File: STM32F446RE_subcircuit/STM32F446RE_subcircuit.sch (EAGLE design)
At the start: 47 parts, among them IC1 74AC126N, IC2 LD117AS33TR, IC3 74AC126N, IC4 74HC04N, IC5 74AC126N, U1 STM32F446RE, X1 MSTBA2, X2 32.768kHz, X3 8MHz

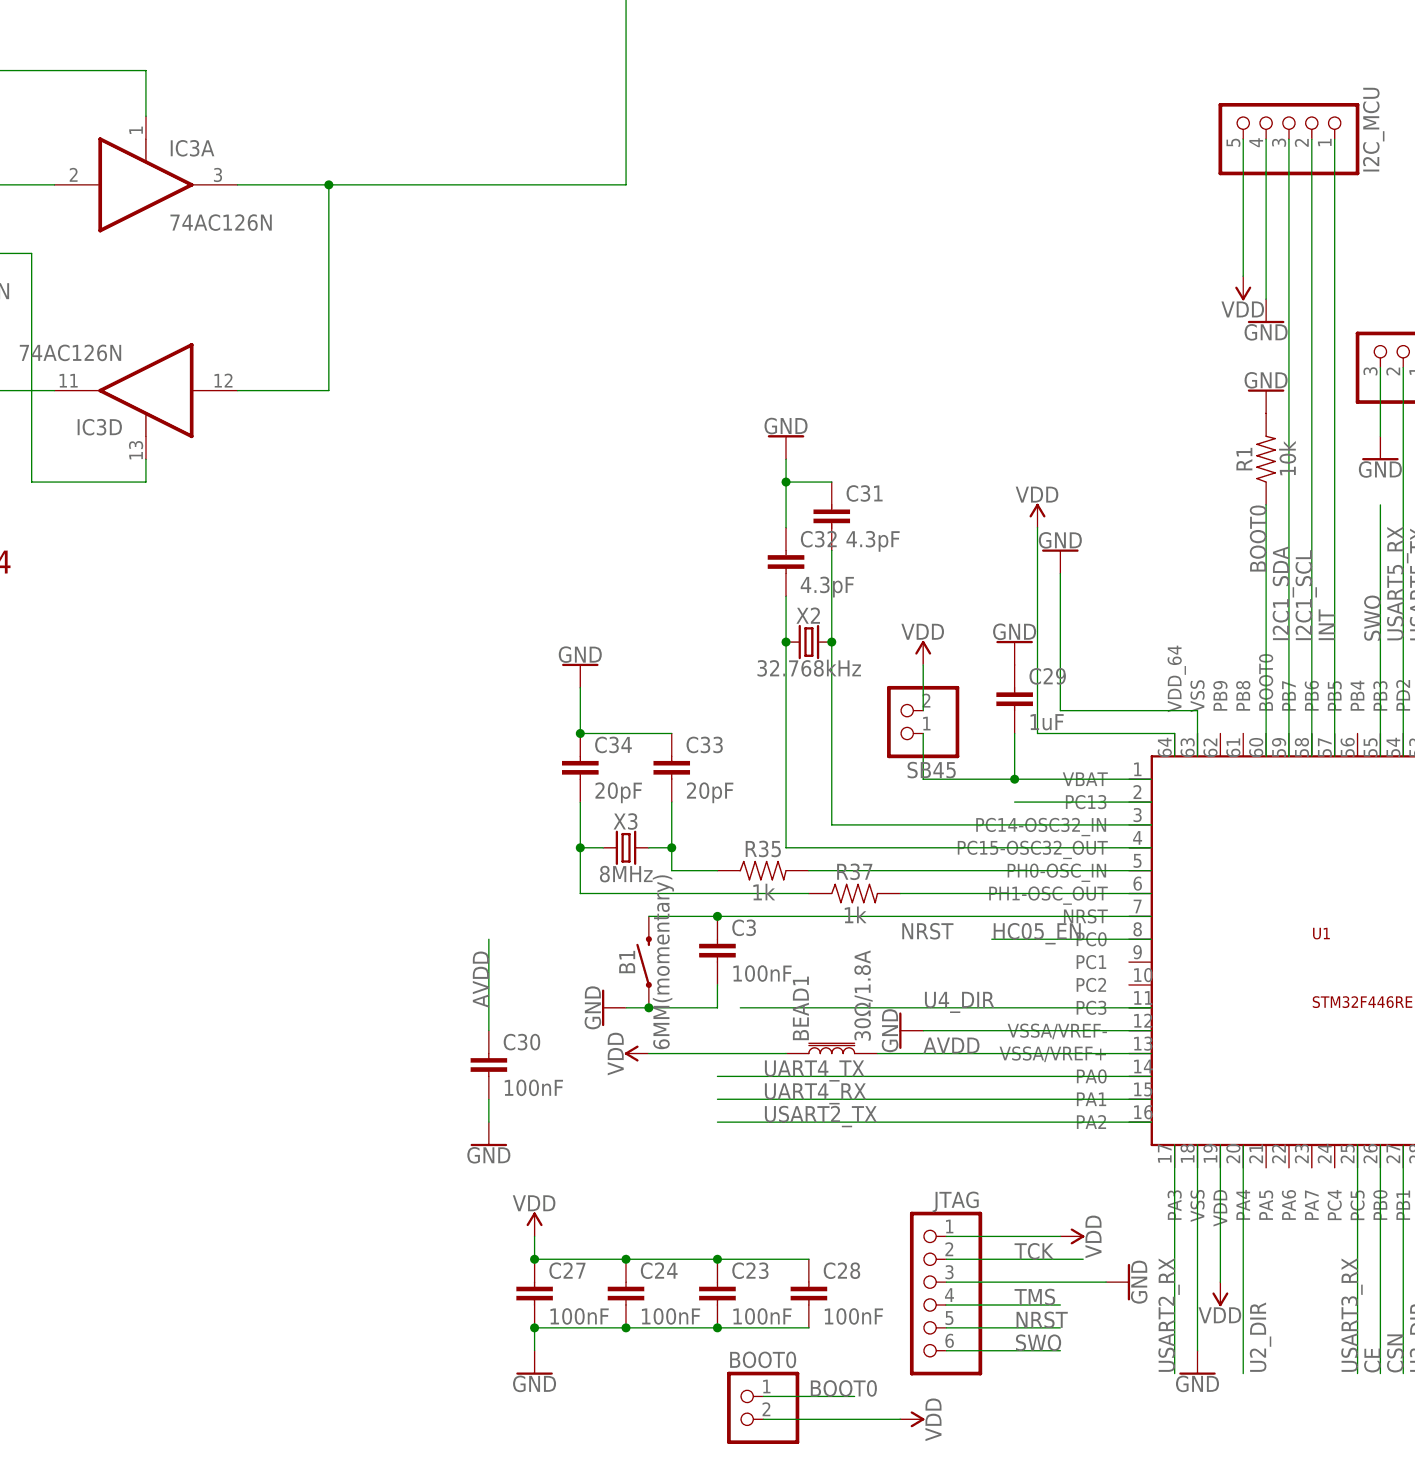
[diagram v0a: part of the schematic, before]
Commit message: Library added, Dip switch and power monitoring header was added
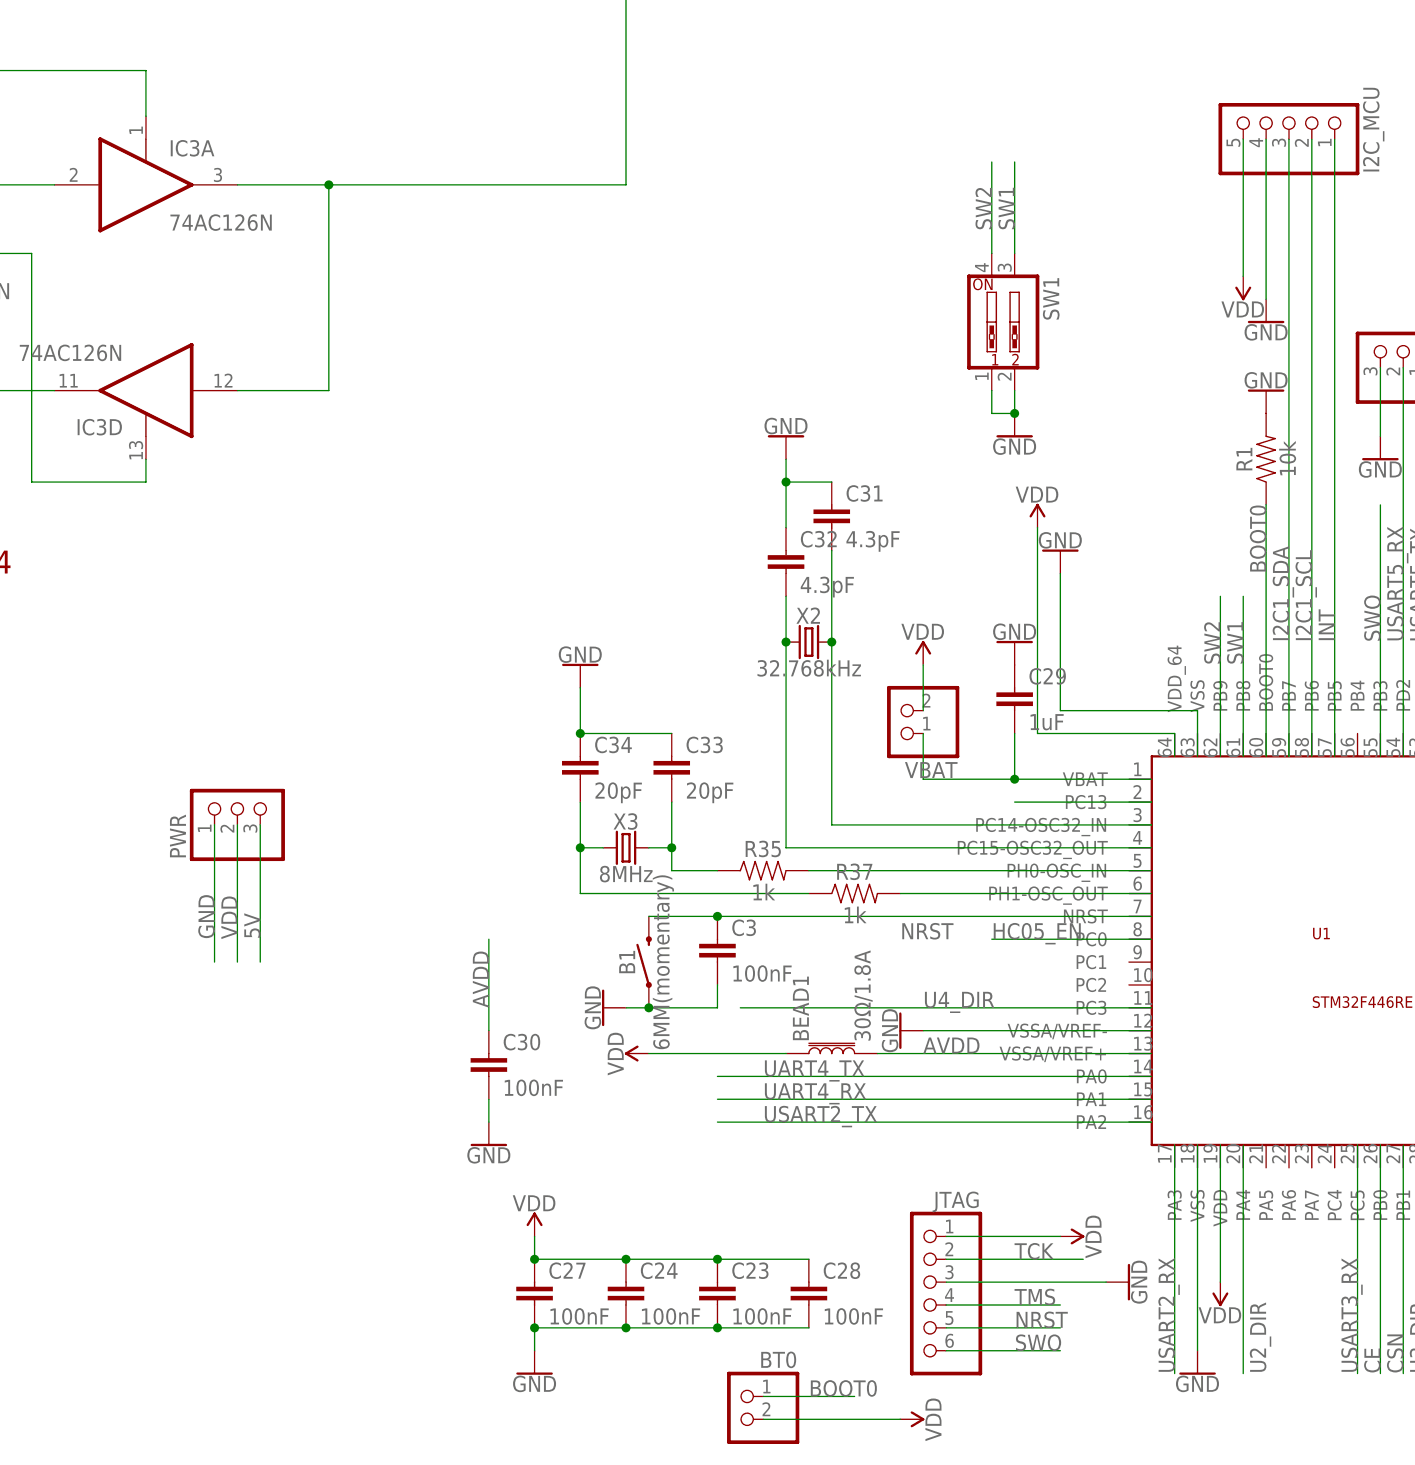
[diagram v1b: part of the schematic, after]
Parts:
- added PWR: (no value), pinhead:PINHD-1X3
- added SW1: (no value), special:SW_DIP-2
- renumbered BOOT0 to BT0, SB45 to VBAT
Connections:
- new net SW1: SW1.3, U1.PB8
- new net SW2: SW1.4, U1.PB9
- net 5V: now also PWR.3
- net GND: now also PWR.1, SW1.1, SW1.2
- net VDD: now also PWR.2
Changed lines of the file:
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@@
 <part name="R35" library="SparkFun-Resistors" deviceset="10KOHM" device="-HORIZ-1/4W-1%" value="1k"/>
 <part name="R37" library="SparkFun-Resistors" deviceset="10KOHM" device="-HORIZ-1/4W-1%" value="1k"/>
-<part name="SB45" library="pinhead" library_urn="urn:adsk.eagle:library:325" deviceset="PINHD-1X2" device="" package3d_urn="urn:adsk.eagle:package:22435/2"/>
+<part name="VBAT" library="pinhead" library_urn="urn:adsk.eagle:library:325" deviceset="PINHD-1X2" device="" package3d_urn="urn:adsk.eagle:package:22435/2"/>
 <part name="SUPPLY1" library="SparkFun-PowerSymbols" deviceset="VDD" device=""/>
 <part name="C29" library="ee2parts" deviceset="C" device="5P" value="1uF"/>
@@
 <part name="JTAG" library="pinhead" library_urn="urn:adsk.eagle:library:325" deviceset="PINHD-1X6" device="" package3d_urn="urn:adsk.eagle:package:22472/2"/>
 <part name="SUPPLY7" library="SparkFun-PowerSymbols" deviceset="VDD" device=""/>
-<part name="BOOT0" library="pinhead" library_urn="urn:adsk.eagle:library:325" deviceset="PINHD-1X2" device="" package3d_urn="urn:adsk.eagle:package:22435/2"/>
+<part name="BT0" library="pinhead" library_urn="urn:adsk.eagle:library:325" deviceset="PINHD-1X2" device="" package3d_urn="urn:adsk.eagle:package:22435/2"/>
 <part name="SUPPLY21" library="SparkFun-PowerSymbols" deviceset="VDD" device=""/>
 <part name="SUPPLY22" library="SparkFun-PowerSymbols" deviceset="VDD" device=""/>
@@
 <part name="NRF" library="pinhead" library_urn="urn:adsk.eagle:library:325" deviceset="PINHD-2X4" device="" package3d_urn="urn:adsk.eagle:package:22461/2"/>
 <part name="C4" library="ee2parts" deviceset="C" device="2.5P" value="100nF"/>
+<part name="SW1" library="special" library_urn="urn:adsk.eagle:library:367" deviceset="SW_DIP-2" device="" package3d_urn="urn:adsk.eagle:package:26654/2"/>
+<part name="GND24" library="SparkFun-PowerSymbols" deviceset="GND" device=""/>
+<part name="PWR" library="pinhead" library_urn="urn:adsk.eagle:library:325" deviceset="PINHD-1X3" device="" package3d_urn="urn:adsk.eagle:package:22458/2"/>
 </parts>
 <sheets>
@@
 <instance part="R35" gate="G$1" x="-63.5" y="10.16"/>
 <instance part="R37" gate="G$1" x="-53.34" y="7.62"/>
-<instance part="SB45" gate="G$1" x="-48.26" y="27.94" rot="R180"/>
+<instance part="VBAT" gate="G$1" x="-48.26" y="27.94" rot="R180"/>
 <instance part="SUPPLY1" gate="VDD" x="-45.72" y="33.02"/>
 <instance part="C29" gate="G$1" x="-35.56" y="27.94"/>
@@
 <instance part="JTAG" gate="A" x="-45.72" y="-38.1" rot="MR0"/>
 <instance part="SUPPLY7" gate="VDD" x="-30.48" y="-30.48" rot="R270"/>
-<instance part="BOOT0" gate="G$1" x="-66.04" y="-50.8" rot="MR0"/>
+<instance part="BT0" gate="G$1" x="-66.04" y="-50.8" rot="MR0"/>
 <instance part="SUPPLY21" gate="VDD" x="-48.26" y="-50.8" rot="R270"/>
 <instance part="SUPPLY22" gate="VDD" x="-12.7" y="-35.56" rot="R180"/>
@@
 <instance part="NRF" gate="A" x="83.82" y="-15.24"/>
 <instance part="C4" gate="G$1" x="86.36" y="-35.56" rot="R90"/>
+<instance part="SW1" gate="G$1" x="-35.56" y="71.12" rot="R270"/>
+<instance part="GND24" gate="1" x="-35.56" y="58.42"/>
+<instance part="PWR" gate="A" x="-121.92" y="17.78" rot="R90"/>
 </instances>
 <busses>
@@
 <junction x="99.06" y="-17.78"/>
 </segment>
+<segment>
+<pinref part="GND24" gate="1" pin="GND"/>
+<pinref part="SW1" gate="G$1" pin="2"/>
+<wire x1="-35.56" y1="60.96" x2="-35.56" y2="63.5" width="0.1524" layer="91"/>
+<pinref part="SW1" gate="G$1" pin="1"/>
+<wire x1="-35.56" y1="60.96" x2="-38.1" y2="60.96" width="0.1524" layer="91"/>
+<wire x1="-38.1" y1="60.96" x2="-38.1" y2="63.5" width="0.1524" layer="91"/>
+<junction x="-35.56" y="60.96"/>
+</segment>
+<segment>
+<pinref part="PWR" gate="A" pin="1"/>
+<wire x1="-124.46" y1="15.24" x2="-124.46" y2="0" width="0.1524" layer="91"/>
+<label x="-124.46" y="2.54" size="1.778" layer="95" rot="R90"/>
+</segment>
 </net>
 <net name="N$4" class="0">
@@
 <segment>
 <pinref part="SUPPLY1" gate="VDD" pin="VDD"/>
-<pinref part="SB45" gate="G$1" pin="2"/>
+<pinref part="VBAT" gate="G$1" pin="2"/>
 <wire x1="-45.72" y1="33.02" x2="-45.72" y2="27.94" width="0.1524" layer="91"/>
 </segment>
@@
 </segment>
 <segment>
-<pinref part="BOOT0" gate="G$1" pin="2"/>
+<pinref part="BT0" gate="G$1" pin="2"/>
 <pinref part="SUPPLY21" gate="VDD" pin="VDD"/>
 <wire x1="-63.5" y1="-50.8" x2="-48.26" y2="-50.8" width="0.1524" layer="91"/>
@@
 <junction x="73.66" y="-17.78"/>
 </segment>
+<segment>
+<pinref part="PWR" gate="A" pin="2"/>
+<wire x1="-121.92" y1="15.24" x2="-121.92" y2="0" width="0.1524" layer="91"/>
+<label x="-121.92" y="2.54" size="1.778" layer="95" rot="R90"/>
+</segment>
 </net>
 <net name="VBAT" class="0">
 <segment>
-<pinref part="SB45" gate="G$1" pin="1"/>
+<pinref part="VBAT" gate="G$1" pin="1"/>
 <wire x1="-45.72" y1="25.4" x2="-45.72" y2="20.32" width="0.1524" layer="91"/>
 <pinref part="U1" gate="G$1" pin="VBAT"/>
@@
 <net name="BOOT0" class="0">
 <segment>
-<pinref part="BOOT0" gate="G$1" pin="1"/>
+<pinref part="BT0" gate="G$1" pin="1"/>
 <wire x1="-63.5" y1="-48.26" x2="-53.34" y2="-48.26" width="0.1524" layer="91"/>
 <label x="-58.42" y="-48.26" size="1.778" layer="95"/>
@@
 <wire x1="33.02" y1="76.2" x2="33.02" y2="63.5" width="0.1524" layer="91"/>
 <label x="33.02" y="63.5" size="1.778" layer="95" rot="R90"/>
+</segment>
+<segment>
+<pinref part="PWR" gate="A" pin="3"/>
+<wire x1="-119.38" y1="15.24" x2="-119.38" y2="0" width="0.1524" layer="91"/>
+<label x="-119.38" y="2.54" size="1.778" layer="95" rot="R90"/>
 </segment>
 </net>
@@
 </segment>
 </net>
+<net name="SW2" class="0">
+<segment>
+<pinref part="U1" gate="G$1" pin="PB9"/>
+<wire x1="-12.7" y1="22.86" x2="-12.7" y2="40.64" width="0.1524" layer="91"/>
+<label x="-12.7" y="33.02" size="1.778" layer="95" rot="R90"/>
+</segment>
+<segment>
+<pinref part="SW1" gate="G$1" pin="4"/>
+<wire x1="-38.1" y1="78.74" x2="-38.1" y2="88.9" width="0.1524" layer="91"/>
+<label x="-38.1" y="81.28" size="1.778" layer="95" rot="R90"/>
+</segment>
+</net>
+<net name="SW1" class="0">
+<segment>
+<pinref part="U1" gate="G$1" pin="PB8"/>
+<wire x1="-10.16" y1="22.86" x2="-10.16" y2="40.64" width="0.1524" layer="91"/>
+<label x="-10.16" y="33.02" size="1.778" layer="95" rot="R90"/>
+</segment>
+<segment>
+<pinref part="SW1" gate="G$1" pin="3"/>
+<wire x1="-35.56" y1="78.74" x2="-35.56" y2="88.9" width="0.1524" layer="91"/>
+<label x="-35.56" y="81.28" size="1.778" layer="95" rot="R90"/>
+</segment>
+</net>

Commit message: final pcb iter. 1
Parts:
- renumbered IC1 to BF1, IC3 to BF2, IC4 to NOT, IC5 to BF3, JP1 to LU, JP2 to RD, JP3 to HH, JP4 to RU, JP6 to LD
